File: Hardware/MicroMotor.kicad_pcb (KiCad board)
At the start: 4 copper layers, 113 x 65.6 mm, 163 parts, among them J1 USB_C_Receptacle_USB2.0, J10 Conn_02x06_Odd_Even, J11 Conn_02x06_Odd_Even, J12 Conn_02x06_Odd_Even, J13 Conn_01x04_Female, J14 Conn_01x04_Female, J15 Conn_01x04_Female, J16 Conn_01x02_Male, J17 Conn_01x02_Female, J2 Conn_01x04_Male, J3 Conn_01x05_Male, J4 Conn_01x04_Male, J5 Conn_01x04_Male, J6 Conn_01x04_Male, J7 Conn_02x06_Odd_Even, J8 Conn_02x06_Odd_Even, J9 Conn_02x06_Odd_Even, Q1 FDB075N15A, Q2 FDB075N15A, Q3 FDB075N15A, Q4 FDB075N15A, Q5 FDB075N15A, Q6 FDB075N15A, SW1 SW_Push, U1 FT230XQ-T, U10 LP2985-3.3, U11 NC7WZ04, U2 STM32F410RBTx, U3 ACSL-6210-00RE, U4 LM2594HVM-12, U5 INA240A3D, U6 INA240A3D, U7 LP2985-5.0, U9 HIP4086ABZ

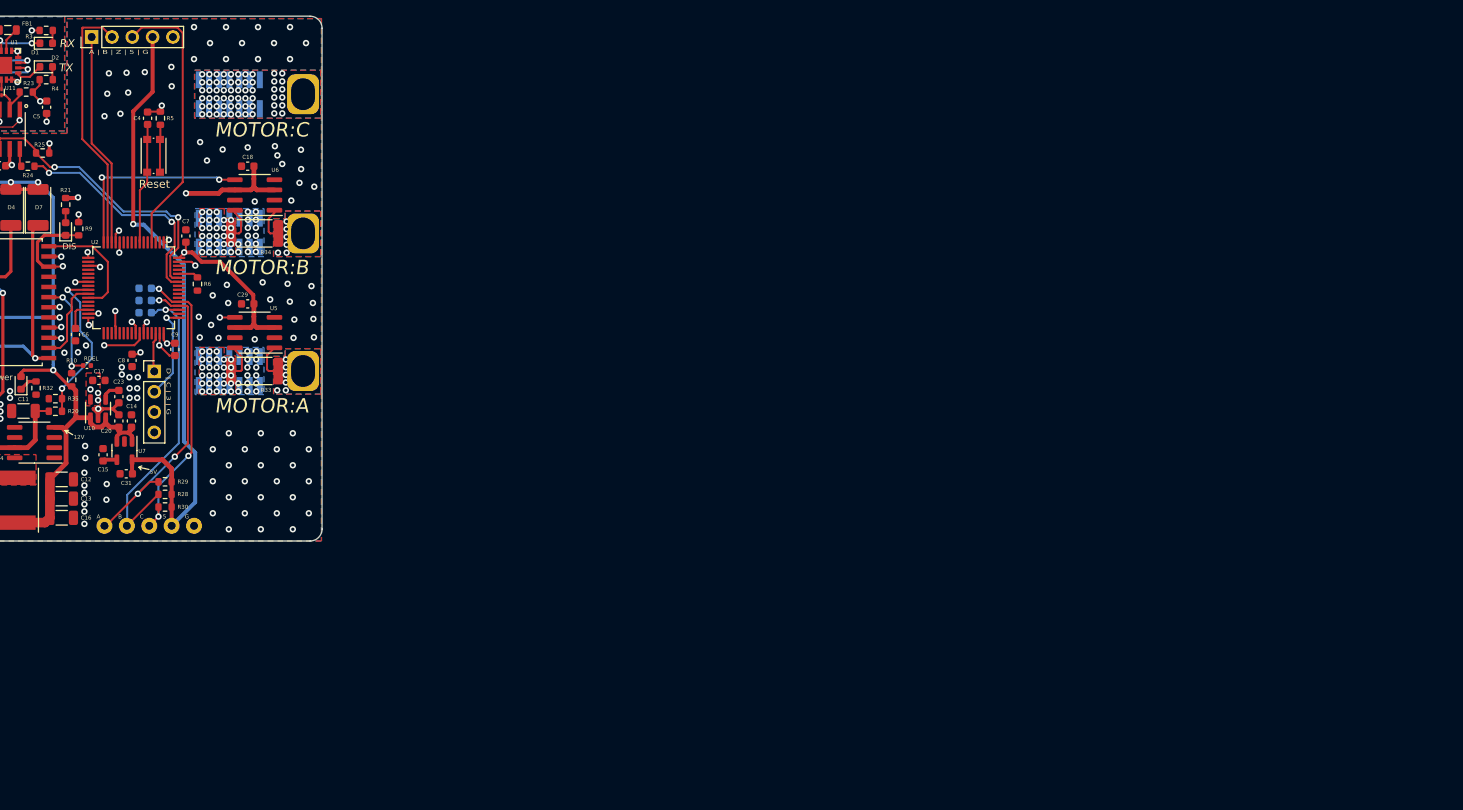
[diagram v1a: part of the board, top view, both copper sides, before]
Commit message: Added UART pads
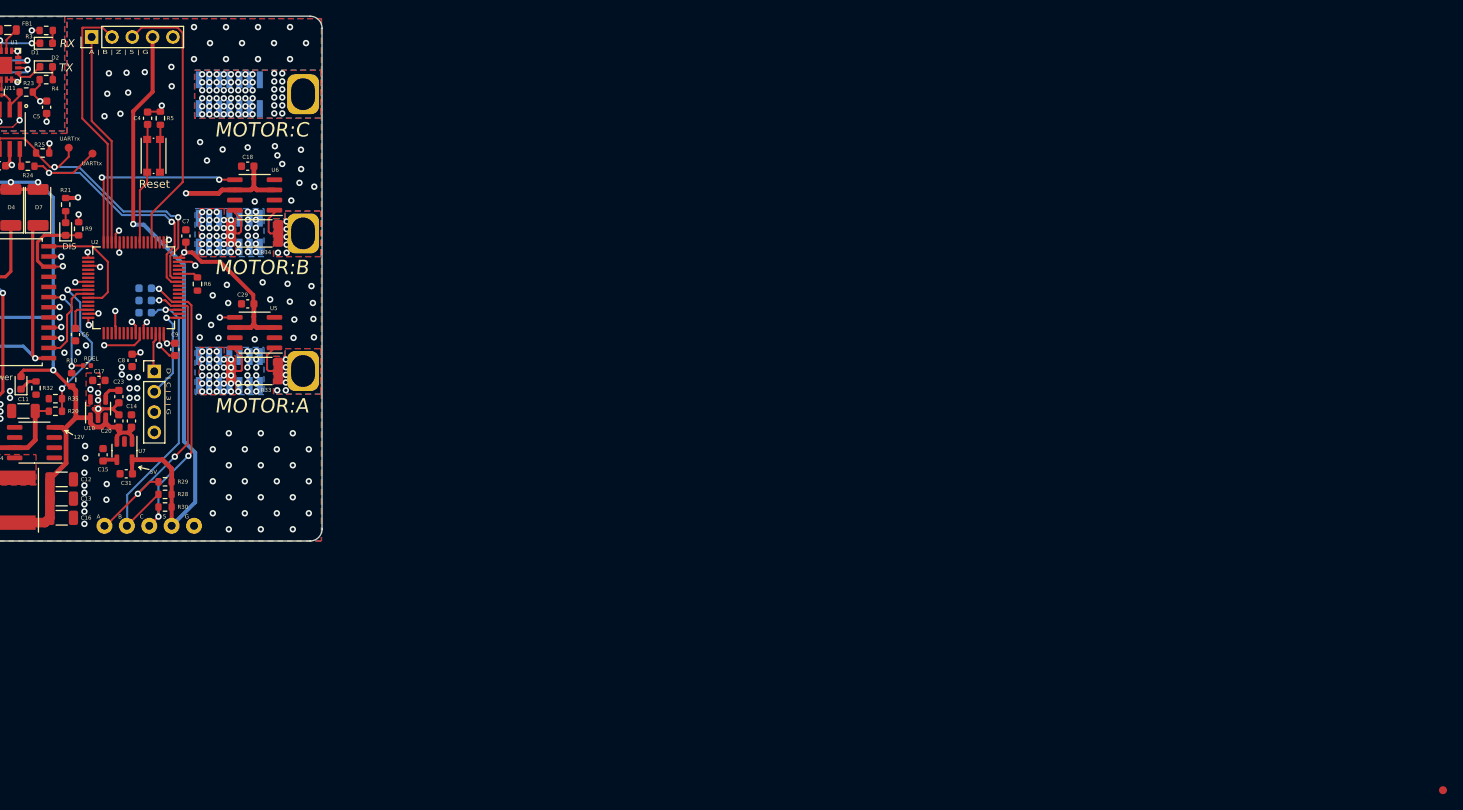
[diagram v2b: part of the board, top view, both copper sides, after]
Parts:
- added ?: , , F.Cu at (171.8, 80.3)
- added UARTrx: TestPoint_Pad_D1.0mm, TestPoint:TestPoint_Pad_D1.0mm, F.Cu at (173.0, 79.1)
- added UARTtx: TestPoint_Pad_D1.0mm, TestPoint:TestPoint_Pad_D1.0mm, F.Cu at (176.0, 79.9)
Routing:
- net USART1_TX: track 29.5 -> 36.0 mm
- net USART1_RX: track 36.8 -> 40.3 mm

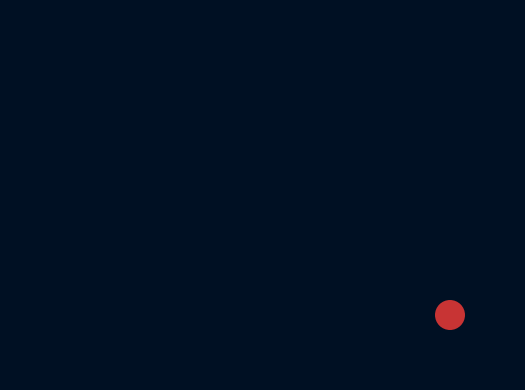
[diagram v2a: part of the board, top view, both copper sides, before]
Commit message: Deleted extra pad
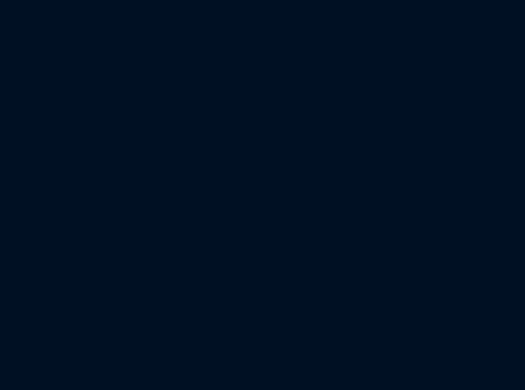
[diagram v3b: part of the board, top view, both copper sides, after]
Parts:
- removed ?: , 
